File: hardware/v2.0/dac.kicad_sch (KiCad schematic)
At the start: 4 parts, among them IC3 LTC2630ISC6-LZ12#TRMPBF, J8 530480210, U1 ECP5U-25F-CABGA256

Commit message: 2CH DAC
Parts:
- removed IC3: LTC2630ISC6-LZ12#TRMPBF, SOT65P210X100-6N, symbol LTC2630ISC6-LZ12#TRMPBF:LTC2630ISC6-LZ12#TRMPBF
- removed J8: 530480210, 530480210:MOLEX_530480210, symbol 530480210:530480210
- added IC4: LTC2622IMS8#PBF, SOP65P490X110-8N, symbol LTC2622IMS8#PBF:LTC2622IMS8#PBF
- added J8: BM04B-ACHSS-A-GAN-TFLFSN, CONN_BM04B-ACHSS-A-GAN-TFLFSN_JST, symbol BM04B_ACHSS_A_GAN_TF_LF__SN:BM04B-ACHSS-A-GAN-TFLFSN
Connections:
- net +3V3: now also IC4.6 (VCC), J8.1
- net GND: now also IC4.7 (GND), J8.4, J8.5, J8.6
- net SCK: now also IC4.2 (SCK)
- net SDI: now also IC4.3 (SDI)
- net ~{CS}(DAC): now also IC4.1 (~{CS}/LD)
- new net VOUT_A: IC4.8 (VOUT_A), J8.2
- new net VOUT_B: IC4.5 (VOUT_B), J8.3
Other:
- moved on the sheet: C82

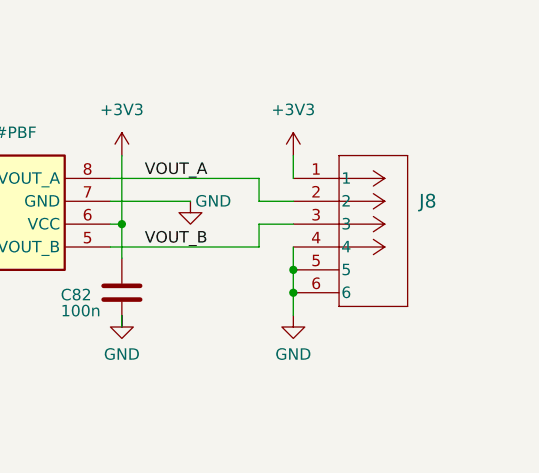
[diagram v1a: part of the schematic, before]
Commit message: Impedance control 100Ohm ADC LVDS diff pairs
Calculated for PCBWay 92th stack with 1OZ inner copper layer
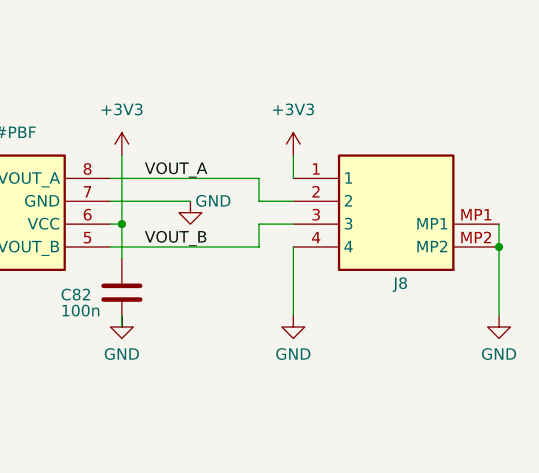
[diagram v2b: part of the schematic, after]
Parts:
- removed J8: BM04B-ACHSS-A-GAN-TFLFSN, CONN_BM04B-ACHSS-A-GAN-TFLFSN_JST, symbol BM04B_ACHSS_A_GAN_TF_LF__SN:BM04B-ACHSS-A-GAN-TFLFSN
- added J8: BM04B-ACHSS-A-GAN-TF_LF__SN_, BM04BACHSSAGANTFLFSN, symbol BM04B-ACHSS-A-GAN-TF_LF__SN_:BM04B-ACHSS-A-GAN-TF_LF__SN_
- IC4: MANUFACTURER (none) -> ADI; MANUFACTURER_PART_NUMBER (none) -> LTC2622IMS8#PBF
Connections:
- net +3V3: now also J8.1
- net GND: now also J8.4, J8.MP1, J8.MP2
- net VOUT_A: now also J8.2
- net VOUT_B: now also J8.3
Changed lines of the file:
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@@
 	)
 	(junction
-		(at 212.09 105.41)
+		(at 234.95 100.33)
 		(diameter 0)
 		(color 0 0 0 0)
 	)
-	(junction
-		(at 212.09 102.87)
-		(diameter 0)
-		(color 0 0 0 0)
-	)
 	(wire
 		(pts
@@
 	(wire
 		(pts
+			(xy 234.95 100.33) (xy 234.95 107.95)
+		)
+		(stroke
+			(width 0)
+			(type default)
+		)
+	)
+	(wire
+		(pts
 			(xy 148.59 95.25) (xy 158.75 95.25)
 		)
@@
 	(wire
 		(pts
-			(xy 212.09 100.33) (xy 212.09 102.87)
+			(xy 212.09 100.33) (xy 212.09 107.95)
 		)
 		(stroke
@@
 	(wire
 		(pts
-			(xy 212.09 105.41) (xy 212.09 107.95)
-		)
-		(stroke
-			(width 0)
-			(type default)
-		)
-	)
-	(wire
-		(pts
 			(xy 193.04 107.95) (xy 193.04 109.22)
 		)
@@
 	(wire
 		(pts
+			(xy 234.95 97.79) (xy 234.95 100.33)
+		)
+		(stroke
+			(width 0)
+			(type default)
+		)
+	)
+	(wire
+		(pts
 			(xy 193.04 101.6) (xy 193.04 97.79)
 		)
@@
 		(pts
 			(xy 132.08 92.71) (xy 158.75 92.71)
-		)
-		(stroke
-			(width 0)
-			(type default)
-		)
-	)
-	(wire
-		(pts
-			(xy 212.09 102.87) (xy 212.09 105.41)
 		)
 		(stroke
@@
 			)
 		)
+		(property "MANUFACTURER" "ADI"
+			(at 158.75 92.71 0)
+			(effects
+				(font
+					(size 1.27 1.27)
+				)
+				(hide yes)
+			)
+		)
+		(property "MANUFACTURER_PART_NUMBER" "LTC2622IMS8#PBF"
+			(at 158.75 92.71 0)
+			(effects
+				(font
+					(size 1.27 1.27)
+				)
+				(hide yes)
+			)
+		)
 		(pin "8"
 		)
@@
 	)
 	(symbol
+		(lib_id "power:GND")
+		(at 234.95 107.95 0)
+		(unit 1)
+		(exclude_from_sim no)
+		(in_bom yes)
+		(on_board yes)
+		(dnp no)
+		(property "Reference" "#PWR0155"
+			(at 234.95 114.3 0)
+			(effects
+				(font
+					(size 1.27 1.27)
+				)
+				(hide yes)
+			)
+		)
+		(property "Value" "GND"
+			(at 234.95 112.268 0)
+			(effects
+				(font
+					(size 1.27 1.27)
+				)
+			)
+		)
+		(property "Footprint" ""
+			(at 234.95 107.95 0)
+			(effects
+				(font
+					(size 1.27 1.27)
+				)
+				(hide yes)
+			)
+		)
+		(property "Datasheet" ""
+			(at 234.95 107.95 0)
+			(effects
+				(font
+					(size 1.27 1.27)
+				)
+				(hide yes)
+			)
+		)
+		(property "Description" "Power symbol creates a global label with name \"GND\" , ground"
+			(at 234.95 107.95 0)
+			(effects
+				(font
+					(size 1.27 1.27)
+				)
+				(hide yes)
+			)
+		)
+		(pin "1"
+		)
+		(instances
+			(project "icepi-zero"
+				(path "/f88da08e-cf42-4d03-a08f-3f602fe6658d/82ea4d67-1fc9-4e6e-a7f0-983b0b32ee19"
+					(reference "#PWR0155")
+					(unit 1)
+				)
+			)
+		)
+	)
+	(symbol
 		(lib_id "power:+3V3")
 		(at 193.04 90.17 0)
@@
 	)
 	(symbol
-		(lib_id "BM04B_ACHSS_A_GAN_TF_LF__SN:BM04B-ACHSS-A-GAN-TFLFSN")
+		(lib_id "BM04B-ACHSS-A-GAN-TF_LF__SN_:BM04B-ACHSS-A-GAN-TF_LF__SN_")
 		(at 212.09 92.71 0)
 		(unit 1)
@@
 		(on_board yes)
 		(dnp no)
-		(fields_autoplaced yes)
 		(property "Reference" "J8"
-			(at 226.06 95.2499 0)
-			(effects
-				(font
-					(size 1.524 1.524)
-				)
-				(justify left)
-			)
-		)
-		(property "Value" "BM04B-ACHSS-A-GAN-TFLFSN"
-			(at 226.06 97.7899 0)
-			(effects
-				(font
-					(size 1.524 1.524)
-				)
-				(justify left)
-				(hide yes)
-			)
-		)
-		(property "Footprint" "CONN_BM04B-ACHSS-A-GAN-TFLFSN_JST"
+			(at 224.028 104.394 0)
+			(effects
+				(font
+					(size 1.27 1.27)
+				)
+			)
+		)
+		(property "Value" "BM04B-ACHSS-A-GAN-TF_LF__SN_"
+			(at 223.52 105.41 0)
+			(effects
+				(font
+					(size 1.27 1.27)
+				)
+				(hide yes)
+			)
+		)
+		(property "Footprint" "BM04BACHSSAGANTFLFSN"
+			(at 231.14 187.63 0)
+			(effects
+				(font
+					(size 1.27 1.27)
+				)
+				(justify left top)
+				(hide yes)
+			)
+		)
+		(property "Datasheet" "https://www.jst-mfg.com/product/pdf/eng/eACH.pdf"
+			(at 231.14 287.63 0)
+			(effects
+				(font
+					(size 1.27 1.27)
+				)
+				(justify left top)
+				(hide yes)
+			)
+		)
+		(property "Description" "CONN HEADER SMD R/A 4POS 1.2MM"
 			(at 212.09 92.71 0)
 			(effects
 				(font
 					(size 1.27 1.27)
-					(italic yes)
-				)
-				(hide yes)
-			)
-		)
-		(property "Datasheet" "BM04B-ACHSS-A-GAN-TFLFSN"
+				)
+				(hide yes)
+			)
+		)
+		(property "Height" "1.4"
+			(at 231.14 487.63 0)
+			(effects
+				(font
+					(size 1.27 1.27)
+				)
+				(justify left top)
+				(hide yes)
+			)
+		)
+		(property "Mouser Part Number" "306-4BACHSSAGANTFL"
+			(at 231.14 587.63 0)
+			(effects
+				(font
+					(size 1.27 1.27)
+				)
+				(justify left top)
+				(hide yes)
+			)
+		)
+		(property "Mouser Price/Stock" "https://www.mouser.co.uk/ProductDetail/JST-Commercial/BM04B-ACHSS-A-GAN-TFLFSN?qs=QpmGXVUTftFsbdf52tFLQQ%3D%3D"
+			(at 231.14 687.63 0)
+			(effects
+				(font
+					(size 1.27 1.27)
+				)
+				(justify left top)
+				(hide yes)
+			)
+		)
+		(property "Manufacturer_Name" "JST (JAPAN SOLDERLESS TERMINALS)"
+			(at 231.14 787.63 0)
+			(effects
+				(font
+					(size 1.27 1.27)
+				)
+				(justify left top)
+				(hide yes)
+			)
+		)
+		(property "Manufacturer_Part_Number" "BM04B-ACHSS-A-GAN-TF(LF)(SN)"
+			(at 231.14 887.63 0)
+			(effects
+				(font
+					(size 1.27 1.27)
+				)
+				(justify left top)
+				(hide yes)
+			)
+		)
+		(property "MANUFACTURER" "JST Commercial"
 			(at 212.09 92.71 0)
 			(effects
 				(font
 					(size 1.27 1.27)
-					(italic yes)
-				)
-				(hide yes)
-			)
-		)
-		(property "Description" ""
+				)
+				(hide yes)
+			)
+		)
+		(property "MANUFACTURER_PART_NUMBER" "M04B-ACHSS-A-GAN-TF(LF)(SN)"
 			(at 212.09 92.71 0)
 			(effects
@@
 			)
 		)
+		(pin "4"
+		)
+		(pin "MP2"
+		)
+		(pin "1"
+		)
+		(pin "2"
+		)
 		(pin "3"
 		)
-		(pin "4"
-		)
-		(pin "2"
-		)
-		(pin "1"
-		)
-		(pin "5"
-		)
-		(pin "6"
+		(pin "MP1"
 		)
 		(instances
-			(project ""
+			(project "icepi-zero"
 				(path "/f88da08e-cf42-4d03-a08f-3f602fe6658d/82ea4d67-1fc9-4e6e-a7f0-983b0b32ee19"
 					(reference "J8")

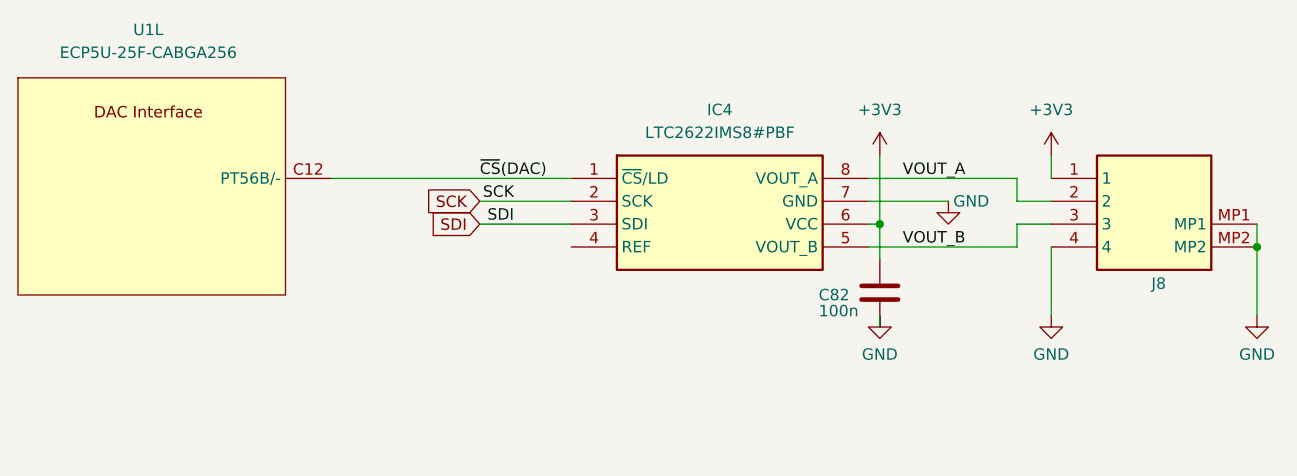
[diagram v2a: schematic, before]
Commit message: DAC voltage reference
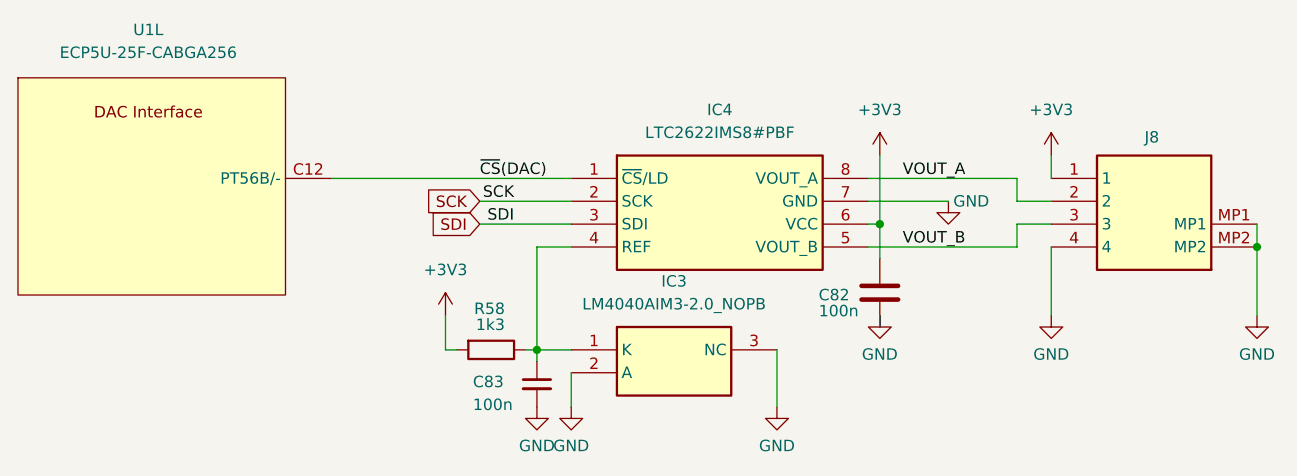
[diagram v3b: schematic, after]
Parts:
- added C83: 100n, Capacitor_SMD:C_0402_1005Metric, symbol Device:C_Small
- added IC3: LM4040AIM3-2.0_NOPB, SOT95P237X95-3N, symbol LM4040AIM3-2_0_NOPB:LM4040AIM3-2.0_NOPB
- added R58: 1k3, Resistor_SMD:R_0402_1005Metric, symbol Device:R
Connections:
- net +3V3: now also R58.2
- net GND: now also C83.2, IC3.2 (A), IC3.3 (NC)
- net at IC4.4 (REF): now also C83.1, IC3.1 (K), R58.1

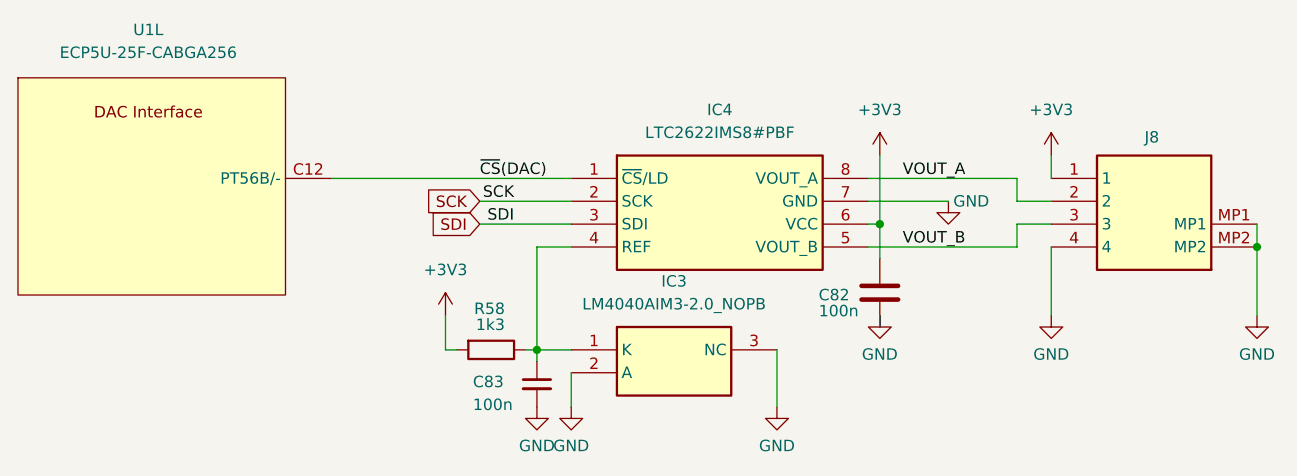
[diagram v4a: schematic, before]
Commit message: Prod ADC power line
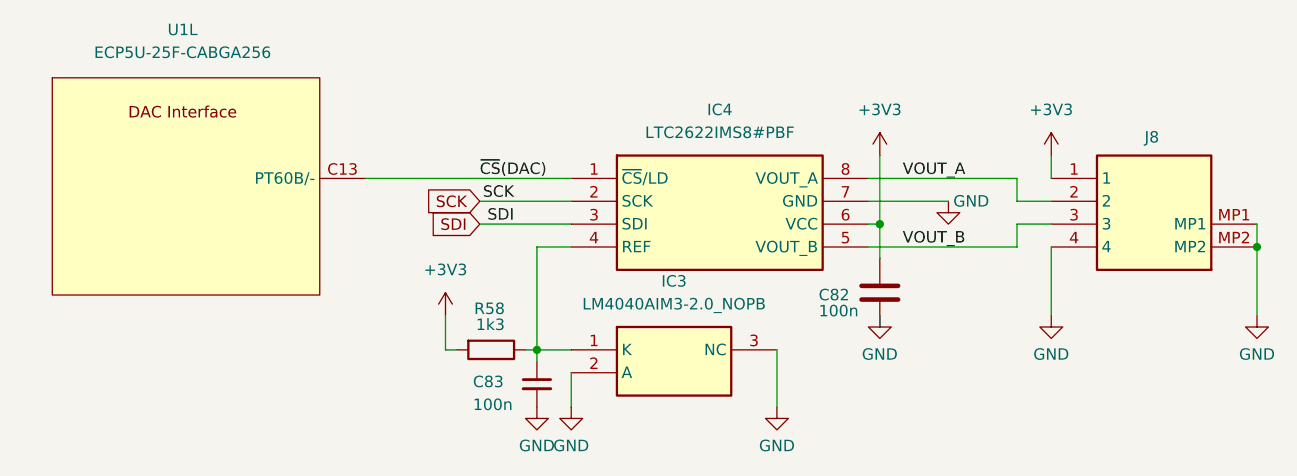
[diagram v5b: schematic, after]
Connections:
- net ~{CS}(DAC): now also U1.C13 (PT60B/-); no longer U1.C12 (PT56B/-)
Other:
- moved on the sheet: U1L
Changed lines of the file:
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@@
 	(wire
 		(pts
-			(xy 132.08 92.71) (xy 158.75 92.71)
+			(xy 181.61 118.11) (xy 181.61 111.76)
 		)
 		(stroke
@@
 	(wire
 		(pts
-			(xy 181.61 118.11) (xy 181.61 111.76)
+			(xy 144.78 107.95) (xy 144.78 111.76)
 		)
 		(stroke
@@
 	(wire
 		(pts
-			(xy 144.78 107.95) (xy 144.78 111.76)
+			(xy 154.94 113.03) (xy 154.94 111.76)
 		)
 		(stroke
@@
 	(wire
 		(pts
-			(xy 154.94 113.03) (xy 154.94 111.76)
+			(xy 144.78 111.76) (xy 146.05 111.76)
 		)
 		(stroke
@@
 	(wire
 		(pts
-			(xy 144.78 111.76) (xy 146.05 111.76)
+			(xy 154.94 111.76) (xy 158.75 111.76)
 		)
 		(stroke
@@
 	(wire
 		(pts
-			(xy 154.94 111.76) (xy 158.75 111.76)
+			(xy 135.89 92.71) (xy 158.75 92.71)
 		)
 		(stroke
@@
 	(symbol
 		(lib_id "icepi-lib:LFE5U-25F-6BG256x")
-		(at 111.76 105.41 0)
+		(at 115.57 105.41 0)
 		(unit 12)
 		(exclude_from_sim no)
@@
 		(dnp no)
 		(property "Reference" "U1"
-			(at 111.76 76.2 0)
+			(at 115.57 76.2 0)
 			(effects
 				(font
@@
 		)
 		(property "Value" "ECP5U-25F-CABGA256"
-			(at 111.76 78.74 0)
+			(at 115.57 78.74 0)
 			(effects
 				(font
@@
 		)
 		(property "Footprint" "Package_BGA:BGA-256_14.0x14.0mm_Layout16x16_P0.8mm_Ball0.45mm_Pad0.32mm_NSMD"
-			(at 109.982 35.052 0)
+			(at 113.792 35.052 0)
 			(effects
 				(font
@@
 		)
 		(property "Datasheet" ""
-			(at 111.76 105.41 0)
+			(at 115.57 105.41 0)
 			(effects
 				(font
@@
 		)
 		(property "Description" "ECP5 FPGA, 24K LUTs, 1.2V, BGA-256"
-			(at 109.982 37.592 0)
+			(at 113.792 37.592 0)
 			(effects
 				(font
@@
 		)
 		(property "MANUFACTURER" "Lattice"
-			(at 111.76 105.41 0)
+			(at 115.57 105.41 0)
 			(effects
 				(font
@@
 		)
 		(property "MANUFACTURER_PART_NUMBER" "LFE5U-25F-6BG256C"
-			(at 111.76 105.41 0)
-			(effects
-				(font
+			(at 115.57 105.41 0)
+			(effects
+				(font
